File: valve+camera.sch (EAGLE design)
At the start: 19 parts, among them X1 RASPI_BOARD_B+#_H, X3 5566-4-RIGHTANGLE

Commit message: Update camera control wiring and relay components
Updated the components driving the relays to be SMD rather than PTH.
The camera control wiring was updated to have relay activating HackHDs
to be located on this board rather than being located on each Camera
Control board (this means that this board is no longer compatible with
rev1 of the Camera Control board and now requires rev2 or newer).
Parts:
- added D5: RED, SparkFun-LED:LED0603
- added Q1: (no value), SparkFun-DiscreteSemi:TRANSISTOR_NPNSOT23-3
- added R5: 1.8k 1/8W, SparkFun-Resistors:RESISTOR0603-RES
- added RELAY3: CAMERA CONTROL, SparkFun-Electromechanical:RELAYPTH
- D1, D2: device SparkFun-DiscreteSemi:DIODEPTH -> SparkFun-DiscreteSemi:DIODESOD123
- D3: value RED -> (none); device SparkFun-LED:LED0603 -> SparkFun-DiscreteSemi:DIODESOD123
- Q2, Q4: device SparkFun-DiscreteSemi:TRANSISTOR_NPNP2N2222A -> SparkFun-DiscreteSemi:TRANSISTOR_NPNSOT23-3
- R1, R2: device SparkFun-Resistors:RESISTORAXIAL-0.3 -> SparkFun-Passives:RESISTOR0603-RES
- R3: value 1.2k 1W -> 1k 1/4W; device SparkFun-Resistors:RESISTOR2512 -> SparkFun-Passives:RESISTOR0603-RES
- R4: value 1.8k 1/8W -> 1.2k 1W; device SparkFun-Resistors:RESISTOR0603-RES -> SparkFun-Resistors:RESISTOR2512
- RELAY1: value Tanks Vent -> TANKS VENT
- RELAY2: value Fuel Valve -> FUEL VALVE
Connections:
- removed net N$1 (its old number): D3.C, R3.1
- new net CIN: RELAY3.MAIN, RJ45-1.1, RJ45-1.3, RJ45-1.5, RJ45-1.7
- new net COUT: RELAY3.NO, RJ45-1.2, RJ45-1.4, RJ45-1.6, RJ45-1.8
- new net N$2: D5.C, R5.1
- new net N$5: Q1.B, R3.2
- new net N$6: D3.A, Q1.C, RELAY3.COIL2
- net 24V: now also D4.A; no longer D3.A
- net 5V: now also D3.C, D5.A, RELAY3.COIL1; no longer D4.A, RJ45-1.4, RJ45-1.5
- net GND: now also Q1.E, R5.2; no longer R4.2, RJ45-1.7, RJ45-1.8
- net GND2: now also R4.2; no longer R3.2
- net WIPI5: now also R3.1; no longer RJ45-1.1, RJ45-1.2
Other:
- moved on the sheet: D4, R3, R4, RJ45-1, RJ45-2, X3-1, X3-2, X3-3, X3-4

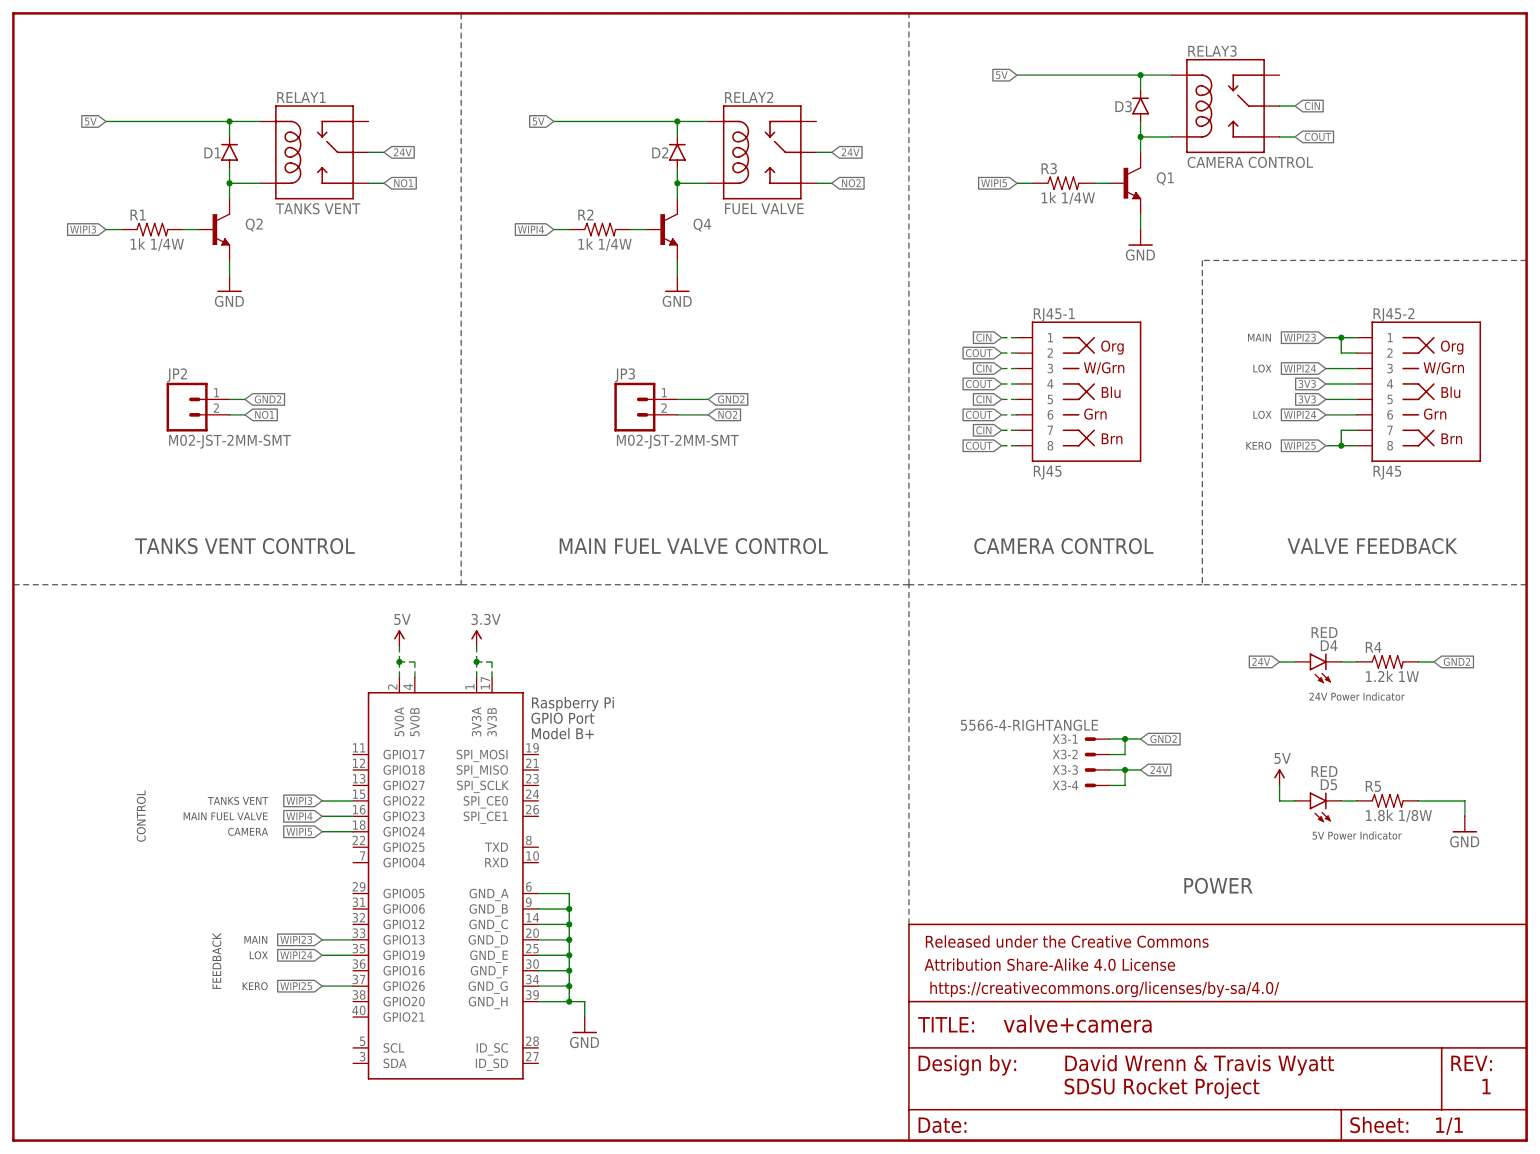
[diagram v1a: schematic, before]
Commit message: Fix feedback port and power thru hole size
Feedback ethernet port was fixed by adding a missing trace.
The 24VDC in thru hole size diameter was increased to adhere to the
datasheet's specifications.
The JST plugs used for valve actuation (tanks vent and main fuel) were
change from SMD to PTH as we had problems with the SMD connectors
breaking off when connecting or disconnecting the plugs.
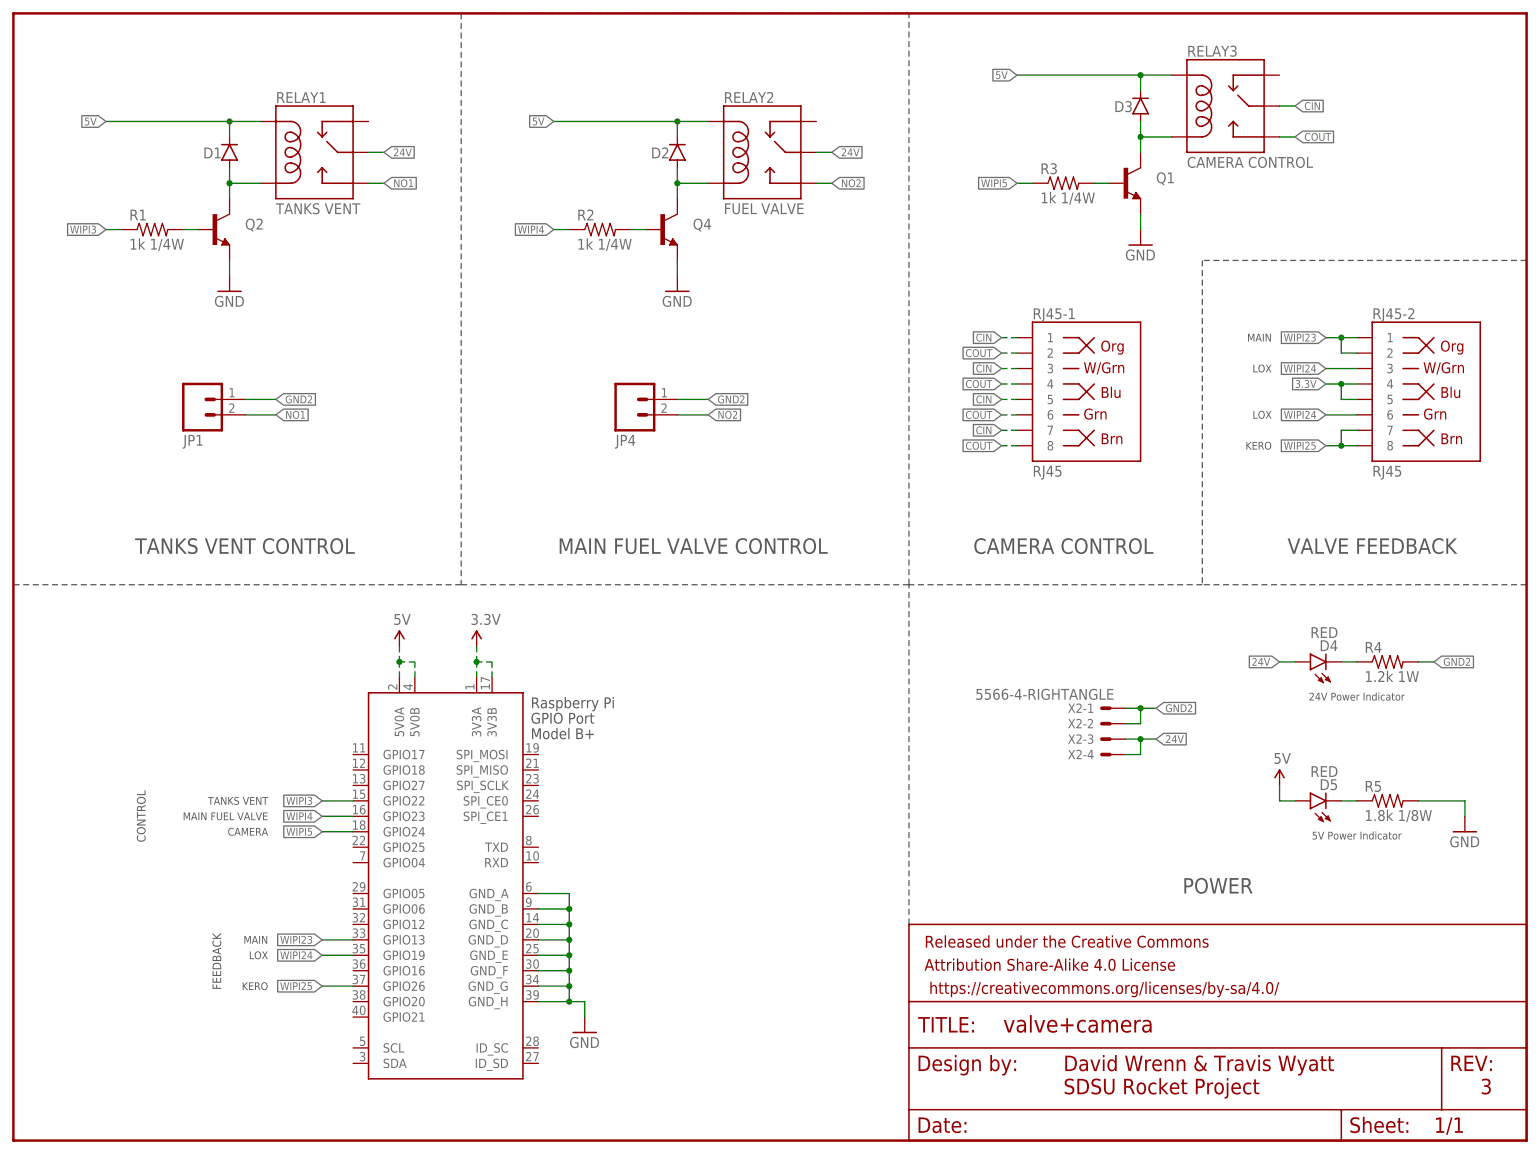
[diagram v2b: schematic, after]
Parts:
- removed JP2, JP3: M02-JST-2MM-SMT, SparkFun-Connectors:M02-JST-2MM-SMT
- removed X3: 5566-4-RIGHTANGLE, SDSURocket-BreakoutBoards:5566-4-RIGHTANGLE
- added JP1, JP4: (no value), SparkFun-Connectors:M02-JST-2-PTH-NO_SILK
- added X2: 5566-4-RIGHTANGLE, SDSURocket-Connectors:5566-4-RIGHTANGLE
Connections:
- removed net 3V3: RJ45-2.4, RJ45-2.5
- net 24V: now also X2-3.S, X2-4.S; no longer X3-3.S, X3-4.S
- net 3.3V: now also RJ45-2.4, RJ45-2.5
- net GND2: now also JP1.1, JP4.1, X2-1.S, X2-2.S; no longer JP2.2, JP3.2, X3-1.S, X3-2.S
- net NO1: now also JP1.2; no longer JP2.1
- net NO2: now also JP4.2; no longer JP3.1
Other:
- note added: "3"
- note removed: "1"
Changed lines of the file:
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@@
 <layer number="56" name="wert" color="7" fill="1" visible="no" active="no"/>
 <layer number="57" name="tCAD" color="7" fill="1" visible="no" active="no"/>
+<layer number="59" name="tCarbon" color="7" fill="1" visible="no" active="no"/>
+<layer number="60" name="bCarbon" color="7" fill="1" visible="no" active="no"/>
 <layer number="90" name="Modules" color="5" fill="1" visible="yes" active="yes"/>
 <layer number="91" name="Nets" color="2" fill="1" visible="yes" active="yes"/>
@@
 <layer number="127" name="_tValues" color="7" fill="1" visible="yes" active="yes"/>
 <layer number="128" name="_bValues" color="7" fill="1" visible="yes" active="yes"/>
+<layer number="129" name="Mask" color="7" fill="1" visible="yes" active="yes"/>
 <layer number="131" name="tAdjust" color="7" fill="1" visible="yes" active="yes"/>
 <layer number="132" name="bAdjust" color="7" fill="1" visible="yes" active="yes"/>
@@
 <layer number="251" name="SMDround" color="12" fill="11" visible="no" active="no"/>
 <layer number="254" name="cooling" color="7" fill="1" visible="yes" active="yes"/>
+<layer number="255" name="routoute" color="7" fill="1" visible="yes" active="yes"/>
 </layers>
 <schematic xreflabel="%F%N/%S.%C%R" xrefpart="/%S.%C%R">
@@
 <part name="SUPPLY1" library="SparkFun-Aesthetics" deviceset="3.3V" device=""/>
 <part name="SUPPLY2" library="SparkFun-Aesthetics" deviceset="5V" device=""/>
-<part name="X3" library="SDSURocket-BreakoutBoards" deviceset="5566-4" device="-RIGHTANGLE"/>
 <part name="D4" library="SparkFun-LED" deviceset="LED" device="0603" value="RED"/>
 <part name="D5" library="SparkFun-LED" deviceset="LED" device="0603" value="RED"/>
@@
 <part name="GND3" library="SparkFun-Aesthetics" deviceset="GND" device=""/>
 <part name="SUPPLY4" library="SparkFun-Aesthetics" deviceset="5V" device=""/>
-<part name="JP2" library="SparkFun-Connectors" deviceset="M02" device="-JST-2MM-SMT"/>
-<part name="JP3" library="SparkFun-Connectors" deviceset="M02" device="-JST-2MM-SMT"/>
 <part name="R3" library="SparkFun-Passives" deviceset="RESISTOR" device="0603-RES" value="1k 1/4W"/>
 <part name="Q1" library="SparkFun-DiscreteSemi" deviceset="TRANSISTOR_NPN" device="SOT23-3"/>
@@
 <part name="GND5" library="SparkFun-Aesthetics" deviceset="GND" device=""/>
 <part name="D3" library="SparkFun-DiscreteSemi" deviceset="DIODE" device="SOD123"/>
+<part name="X2" library="SDSURocket-Connectors" deviceset="5566-4" device="-RIGHTANGLE"/>
+<part name="JP4" library="SparkFun-Connectors" deviceset="M02" device="-JST-2-PTH-NO_SILK"/>
+<part name="JP1" library="SparkFun-Connectors" deviceset="M02" device="-JST-2-PTH-NO_SILK"/>
 </parts>
 <sheets>
@@
 <text x="172.72" y="96.52" size="2.54" layer="97" align="bottom-center">CAMERA CONTROL</text>
 <text x="198.12" y="40.64" size="2.54" layer="97" align="bottom-center">POWER</text>
-<text x="241.3" y="7.62" size="2.54" layer="94">1</text>
+<text x="241.3" y="7.62" size="2.54" layer="94">3</text>
 <text x="172.72" y="12.7" size="2.54" layer="94" align="center-left">David Wrenn &amp; Travis Wyatt</text>
 <text x="172.72" y="8.89" size="2.54" layer="94" align="center-left">SDSU Rocket Project</text>
@@
 <instance part="SUPPLY1" gate="G$1" x="76.2" y="81.28"/>
 <instance part="SUPPLY2" gate="G$1" x="63.5" y="81.28"/>
-<instance part="X3" gate="-1" x="177.8" y="66.04" rot="MR0"/>
-<instance part="X3" gate="-2" x="177.8" y="63.5" rot="MR0"/>
-<instance part="X3" gate="-3" x="177.8" y="60.96" rot="MR0"/>
-<instance part="X3" gate="-4" x="177.8" y="58.42" rot="MR0"/>
 <instance part="D4" gate="G$1" x="213.36" y="78.74" rot="R90"/>
 <instance part="D5" gate="G$1" x="213.36" y="55.88" rot="R90"/>
@@
 <instance part="GND3" gate="1" x="238.76" y="50.8"/>
 <instance part="SUPPLY4" gate="G$1" x="208.28" y="58.42"/>
-<instance part="JP2" gate="G$1" x="27.94" y="119.38"/>
-<instance part="JP3" gate="G$1" x="101.6" y="119.38"/>
 <instance part="R3" gate="G$1" x="172.72" y="157.48"/>
 <instance part="Q1" gate="G$1" x="182.88" y="157.48"/>
@@
 <attribute name="VALUE" x="187.7314" y="172.72" size="1.778" layer="96" rot="R90"/>
 </instance>
+<instance part="X2" gate="-1" x="180.34" y="71.12" rot="MR0"/>
+<instance part="X2" gate="-2" x="180.34" y="68.58" rot="MR0"/>
+<instance part="X2" gate="-3" x="180.34" y="66.04" rot="MR0"/>
+<instance part="X2" gate="-4" x="180.34" y="63.5" rot="MR0"/>
+<instance part="JP4" gate="G$1" x="101.6" y="121.92" rot="MR180"/>
+<instance part="JP1" gate="G$1" x="30.48" y="121.92" rot="MR180"/>
 </instances>
 <busses>
@@
 </segment>
 <segment>
-<pinref part="X3" gate="-3" pin="S"/>
-<wire x1="180.34" y1="60.96" x2="182.88" y2="60.96" width="0.1524" layer="91"/>
-<pinref part="X3" gate="-4" pin="S"/>
-<wire x1="182.88" y1="60.96" x2="185.42" y2="60.96" width="0.1524" layer="91"/>
-<wire x1="180.34" y1="58.42" x2="182.88" y2="58.42" width="0.1524" layer="91"/>
-<wire x1="182.88" y1="58.42" x2="182.88" y2="60.96" width="0.1524" layer="91"/>
-<junction x="182.88" y="60.96"/>
-<label x="185.42" y="60.96" size="1.27" layer="95" xref="yes"/>
-</segment>
-<segment>
 <pinref part="D4" gate="G$1" pin="A"/>
 <wire x1="210.82" y1="78.74" x2="208.28" y2="78.74" width="0.1524" layer="91"/>
 <label x="208.28" y="78.74" size="1.27" layer="95" rot="MR0" xref="yes"/>
 </segment>
+<segment>
+<pinref part="X2" gate="-3" pin="S"/>
+<wire x1="182.88" y1="66.04" x2="185.42" y2="66.04" width="0.1524" layer="91"/>
+<pinref part="X2" gate="-4" pin="S"/>
+<wire x1="185.42" y1="66.04" x2="187.96" y2="66.04" width="0.1524" layer="91"/>
+<wire x1="182.88" y1="63.5" x2="185.42" y2="63.5" width="0.1524" layer="91"/>
+<wire x1="185.42" y1="63.5" x2="185.42" y2="66.04" width="0.1524" layer="91"/>
+<junction x="185.42" y="66.04"/>
+<label x="187.96" y="66.04" size="1.27" layer="95" xref="yes"/>
+</segment>
 </net>
 <net name="NO1" class="0">
@@
 </segment>
 <segment>
-<pinref part="JP2" gate="G$1" pin="1"/>
-<wire x1="35.56" y1="119.38" x2="38.1" y2="119.38" width="0.1524" layer="91"/>
-<label x="38.1" y="119.38" size="1.27" layer="95" xref="yes"/>
+<pinref part="JP1" gate="G$1" pin="2"/>
+<wire x1="38.1" y1="119.38" x2="43.18" y2="119.38" width="0.1524" layer="91"/>
+<label x="43.18" y="119.38" size="1.27" layer="95" xref="yes"/>
 </segment>
 </net>
@@
 </segment>
 <segment>
-<pinref part="JP3" gate="G$1" pin="1"/>
+<pinref part="JP4" gate="G$1" pin="2"/>
 <wire x1="109.22" y1="119.38" x2="114.3" y2="119.38" width="0.1524" layer="91"/>
 <label x="114.3" y="119.38" size="1.27" layer="95" xref="yes"/>
@@
 <junction x="76.2" y="78.74"/>
 </segment>
+<segment>
+<pinref part="RJ45-2" gate="JP1" pin="4"/>
+<wire x1="220.98" y1="124.46" x2="218.44" y2="124.46" width="0.1524" layer="91"/>
+<label x="215.9" y="124.46" size="1.27" layer="95" rot="MR0" xref="yes"/>
+<pinref part="RJ45-2" gate="JP1" pin="5"/>
+<wire x1="218.44" y1="124.46" x2="215.9" y2="124.46" width="0.1524" layer="91"/>
+<wire x1="220.98" y1="121.92" x2="218.44" y2="121.92" width="0.1524" layer="91"/>
+<wire x1="218.44" y1="121.92" x2="218.44" y2="124.46" width="0.1524" layer="91"/>
+<junction x="218.44" y="124.46"/>
+</segment>
 </net>
 <net name="GND2" class="0">
-<segment>
-<pinref part="X3" gate="-1" pin="S"/>
-<wire x1="180.34" y1="66.04" x2="182.88" y2="66.04" width="0.1524" layer="91"/>
-<pinref part="X3" gate="-2" pin="S"/>
-<wire x1="182.88" y1="66.04" x2="185.42" y2="66.04" width="0.1524" layer="91"/>
-<wire x1="180.34" y1="63.5" x2="182.88" y2="63.5" width="0.1524" layer="91"/>
-<wire x1="182.88" y1="63.5" x2="182.88" y2="66.04" width="0.1524" layer="91"/>
-<junction x="182.88" y="66.04"/>
-<label x="185.42" y="66.04" size="1.27" layer="95" xref="yes"/>
-</segment>
 <segment>
 <pinref part="R4" gate="G$1" pin="2"/>
@@
 </segment>
 <segment>
-<pinref part="JP2" gate="G$1" pin="2"/>
-<wire x1="35.56" y1="121.92" x2="38.1" y2="121.92" width="0.1524" layer="91"/>
-<label x="38.1" y="121.92" size="1.27" layer="95" xref="yes"/>
-</segment>
-<segment>
-<pinref part="JP3" gate="G$1" pin="2"/>
+<pinref part="X2" gate="-1" pin="S"/>
+<wire x1="182.88" y1="71.12" x2="185.42" y2="71.12" width="0.1524" layer="91"/>
+<pinref part="X2" gate="-2" pin="S"/>
+<wire x1="185.42" y1="71.12" x2="187.96" y2="71.12" width="0.1524" layer="91"/>
+<wire x1="182.88" y1="68.58" x2="185.42" y2="68.58" width="0.1524" layer="91"/>
+<wire x1="185.42" y1="68.58" x2="185.42" y2="71.12" width="0.1524" layer="91"/>
+<junction x="185.42" y="71.12"/>
+<label x="187.96" y="71.12" size="1.27" layer="95" xref="yes"/>
+</segment>
+<segment>
+<pinref part="JP4" gate="G$1" pin="1"/>
 <wire x1="109.22" y1="121.92" x2="114.3" y2="121.92" width="0.1524" layer="91"/>
 <label x="114.3" y="121.92" size="1.27" layer="95" xref="yes"/>
+</segment>
+<segment>
+<pinref part="JP1" gate="G$1" pin="1"/>
+<wire x1="38.1" y1="121.92" x2="43.18" y2="121.92" width="0.1524" layer="91"/>
+<label x="43.18" y="121.92" size="1.27" layer="95" xref="yes"/>
 </segment>
 </net>
@@
 </segment>
 </net>
-<net name="3V3" class="0">
-<segment>
-<pinref part="RJ45-2" gate="JP1" pin="4"/>
-<wire x1="220.98" y1="124.46" x2="215.9" y2="124.46" width="0.1524" layer="91"/>
-<label x="215.9" y="124.46" size="1.27" layer="95" rot="MR0" xref="yes"/>
-</segment>
-<segment>
-<pinref part="RJ45-2" gate="JP1" pin="5"/>
-<wire x1="220.98" y1="121.92" x2="215.9" y2="121.92" width="0.1524" layer="91"/>
-<label x="215.9" y="121.92" size="1.27" layer="95" rot="MR0" xref="yes"/>
-</segment>
-</net>
